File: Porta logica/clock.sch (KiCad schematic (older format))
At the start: 12 parts, among them P5 Clock, U6 74HC00, U7 LM555N

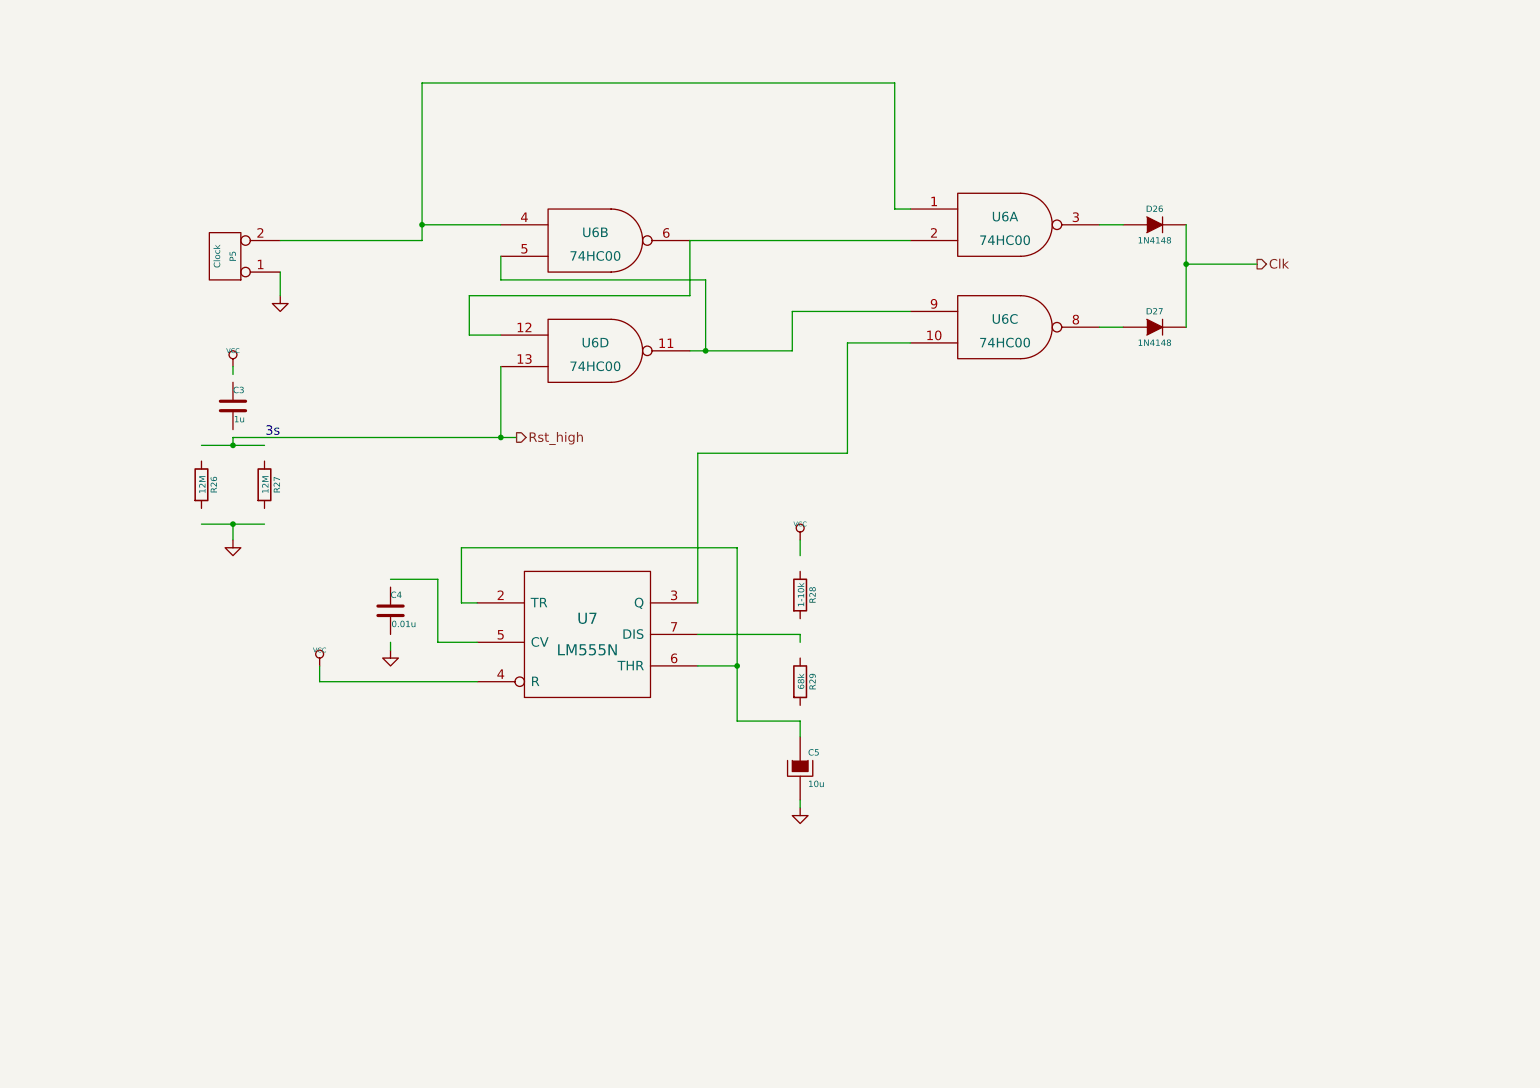
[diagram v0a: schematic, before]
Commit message: correzione bug, migliorie grafiche
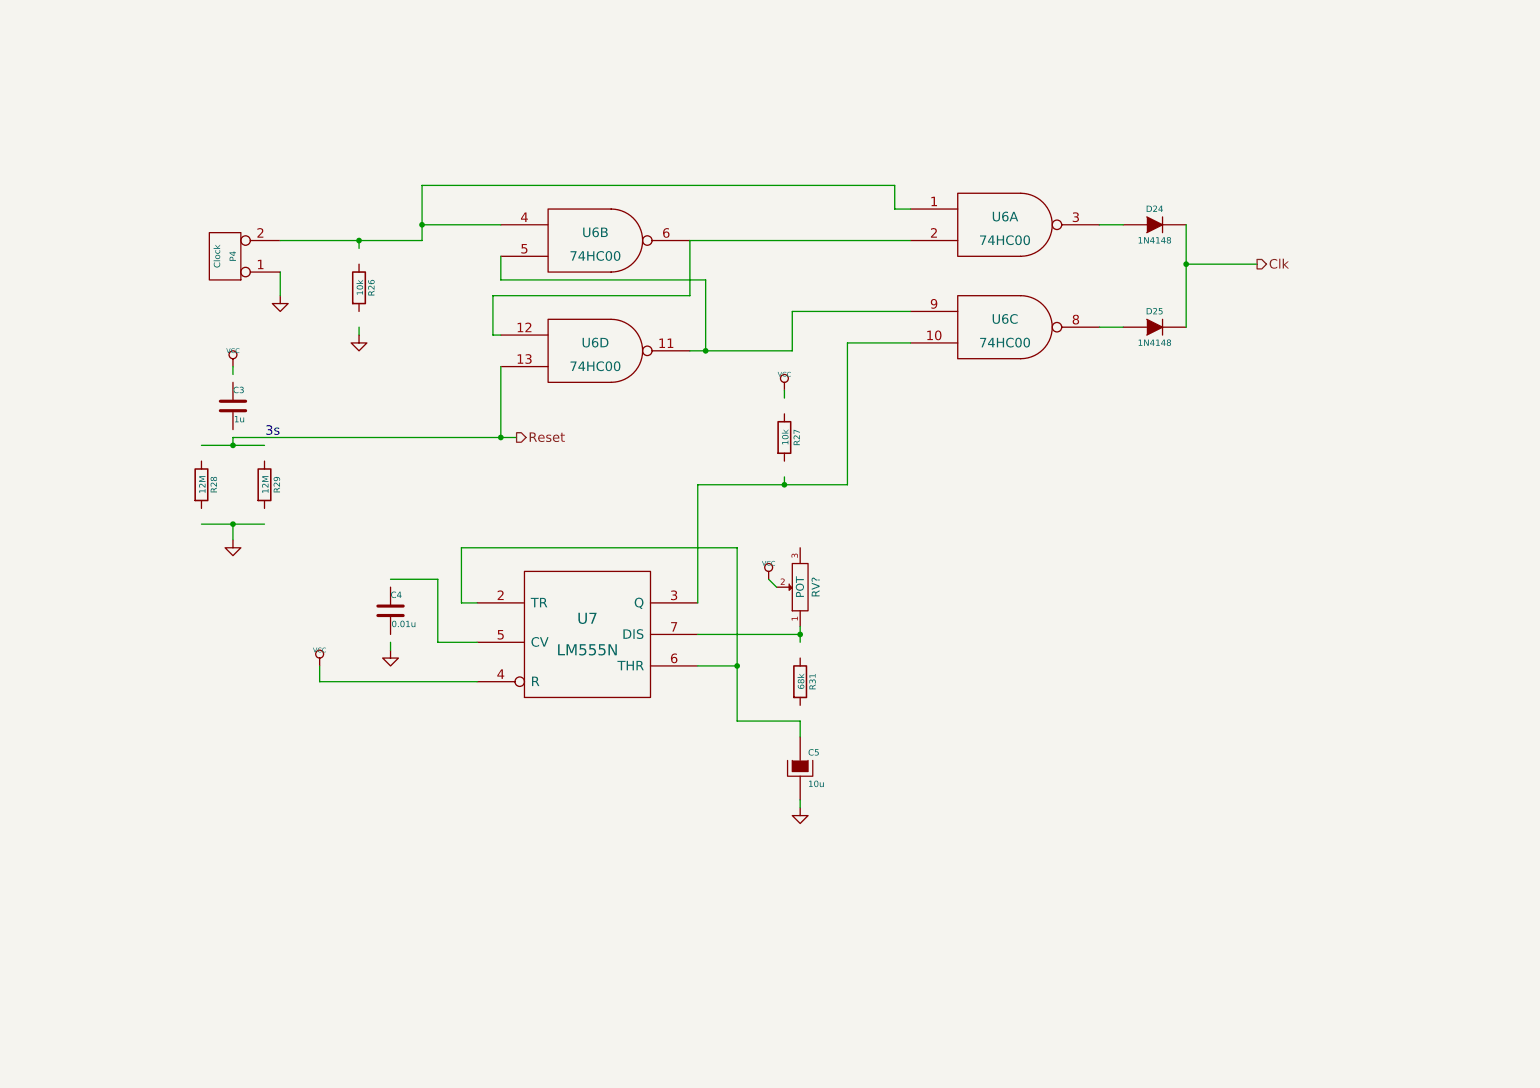
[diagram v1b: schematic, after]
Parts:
- removed R28: 1-10k, ~, symbol R
- added R26, R27: 10k, ~, symbol R
- added RV?: POT, ~, symbol POT
- renumbered D26 to D24, D27 to D25, P5 to P4, R26 to R28, R27 to R29, R29 to R31
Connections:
- net labels added: Reset
- net labels removed: Rst_high
- wire segments 50 -> 54
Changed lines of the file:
@@
 $Descr A4 11693 8268
 encoding utf-8
-Sheet 3 3
+Sheet 2 3
 Title ""
 Date "20 may 2015"
@@
 $EndComp
 $Comp
-L VCC #PWR021
+L VCC #PWR019
 U 1 1 555C3841
 P 3250 4650
-F 0 "#PWR021" H 3250 4750 30  0001 C CNN
+F 0 "#PWR019" H 3250 4750 30  0001 C CNN
 F 1 "VCC" H 3250 4750 30  0000 C CNN
 F 2 "" H 3250 4650 60  0000 C CNN
@@
 $EndComp
 $Comp
-L GND #PWR022
+L GND #PWR020
 U 1 1 555C384D
 P 3700 4550
-F 0 "#PWR022" H 3700 4550 30  0001 C CNN
+F 0 "#PWR020" H 3700 4550 30  0001 C CNN
 F 1 "GND" H 3700 4480 30  0001 C CNN
 F 2 "" H 3700 4550 60  0000 C CNN
@@
 $EndComp
 $Comp
-L R R29
+L R R31
 U 1 1 555C3853
 P 6300 4750
-F 0 "R29" V 6380 4750 40  0000 C CNN
+F 0 "R31" V 6380 4750 40  0000 C CNN
 F 1 "68k" V 6307 4751 40  0000 C CNN
 F 2 "~" V 6230 4750 30  0000 C CNN
 F 3 "~" H 6300 4750 30  0000 C CNN
 	1    6300 4750
-	1    0    0    -1
-$EndComp
-$Comp
-L R R28
-U 1 1 555C3859
-P 6300 4200
-F 0 "R28" V 6380 4200 40  0000 C CNN
-F 1 "1-10k" V 6307 4201 40  0000 C CNN
-F 2 "~" V 6230 4200 30  0000 C CNN
-F 3 "~" H 6300 4200 30  0000 C CNN
-	1    6300 4200
 	1    0    0    -1
 $EndComp
@@
 $EndComp
 $Comp
-L VCC #PWR023
+L VCC #PWR021
 U 1 1 555C3865
-P 6300 3850
-F 0 "#PWR023" H 6300 3950 30  0001 C CNN
-F 1 "VCC" H 6300 3950 30  0000 C CNN
-F 2 "" H 6300 3850 60  0000 C CNN
-F 3 "" H 6300 3850 60  0000 C CNN
-	1    6300 3850
-	1    0    0    -1
-$EndComp
-$Comp
-L GND #PWR024
+P 6100 4100
+F 0 "#PWR021" H 6100 4200 30  0001 C CNN
+F 1 "VCC" H 6100 4200 30  0000 C CNN
+F 2 "" H 6100 4100 60  0000 C CNN
+F 3 "" H 6100 4100 60  0000 C CNN
+	1    6100 4100
+	1    0    0    -1
+$EndComp
+$Comp
+L GND #PWR022
 U 1 1 555C386B
 P 6300 5550
-F 0 "#PWR024" H 6300 5550 30  0001 C CNN
+F 0 "#PWR022" H 6300 5550 30  0001 C CNN
 F 1 "GND" H 6300 5480 30  0001 C CNN
 F 2 "" H 6300 5550 60  0000 C CNN
@@
 	6300 5000 6300 5100
 Wire Wire Line
-	6300 4500 6300 4450
+	6300 4400 6300 4500
 Wire Wire Line
 	6300 5500 6300 5550
 Wire Wire Line
-	6300 3950 6300 3850
+	6150 4150 6100 4100
 Wire Wire Line
 	6300 4450 5650 4450
@@
 Connection ~ 5900 4650
 Wire Wire Line
-	5650 3300 5650 4250
-$Comp
-L CONN_2 P5
+	5650 3500 5650 4250
+$Comp
+L CONN_2 P4
 U 1 1 555C3887
 P 2650 2050
-F 0 "P5" V 2600 2050 40  0000 C CNN
+F 0 "P4" V 2600 2050 40  0000 C CNN
 F 1 "Clock" V 2700 2050 40  0000 C CNN
 F 2 "" H 2650 2050 60  0000 C CNN
@@
 $EndComp
 $Comp
-L GND #PWR025
+L GND #PWR023
 U 1 1 555C5E35
 P 3000 2300
-F 0 "#PWR025" H 3000 2300 30  0001 C CNN
+F 0 "#PWR023" H 3000 2300 30  0001 C CNN
 F 1 "GND" H 3000 2230 30  0001 C CNN
 F 2 "" H 3000 2300 60  0000 C CNN
@@
 	3900 1950 3000 1950
 Wire Wire Line
-	3900 950  3900 1950
-Wire Wire Line
-	3900 950  6900 950
-Wire Wire Line
-	6900 950  6900 1750
+	3900 1600 3900 1950
+Wire Wire Line
+	3900 1600 6900 1600
+Wire Wire Line
+	6900 1600 6900 1750
 Wire Wire Line
 	6900 1750 7000 1750
@@
 	5600 1950 5600 2300
 Wire Wire Line
-	5600 2300 4200 2300
-Wire Wire Line
-	4200 2300 4200 2550
-Wire Wire Line
-	4200 2550 4400 2550
+	5600 2300 4350 2300
+Wire Wire Line
+	4350 2300 4350 2550
+Wire Wire Line
+	4350 2550 4400 2550
 Wire Wire Line
 	4400 2050 4400 2200
@@
 	7000 2600 6600 2600
 Wire Wire Line
-	6600 2600 6600 3300
-Wire Wire Line
-	6600 3300 5650 3300
-$Comp
-L VCC #PWR026
+	6600 2600 6600 3500
+Wire Wire Line
+	6600 3500 5650 3500
+$Comp
+L VCC #PWR024
 U 1 1 555C5F80
 P 2700 2750
-F 0 "#PWR026" H 2700 2850 30  0001 C CNN
+F 0 "#PWR024" H 2700 2850 30  0001 C CNN
 F 1 "VCC" H 2700 2850 30  0000 C CNN
 F 2 "" H 2700 2750 60  0000 C CNN
@@
 $EndComp
 $Comp
-L GND #PWR027
+L GND #PWR025
 U 1 1 555C5F8F
 P 2700 3850
-F 0 "#PWR027" H 2700 3850 30  0001 C CNN
+F 0 "#PWR025" H 2700 3850 30  0001 C CNN
 F 1 "GND" H 2700 3780 30  0001 C CNN
 F 2 "" H 2700 3850 60  0000 C CNN
@@
 Clk
 Text HLabel 4500 3200 2    60   Output ~ 0
-Rst_high
+Reset
 Connection ~ 4400 3200
 $Comp
-L DIODE D26
+L DIODE D24
 U 1 1 555C7B93
 P 8550 1850
-F 0 "D26" H 8550 1950 40  0000 C CNN
+F 0 "D24" H 8550 1950 40  0000 C CNN
 F 1 "1N4148" H 8550 1750 40  0000 C CNN
 F 2 "~" H 8550 1850 60  0000 C CNN
@@
 $EndComp
 $Comp
-L DIODE D27
+L DIODE D25
 U 1 1 555C7BA5
 P 8550 2500
-F 0 "D27" H 8550 2600 40  0000 C CNN
+F 0 "D25" H 8550 2600 40  0000 C CNN
 F 1 "1N4148" H 8550 2400 40  0000 C CNN
 F 2 "~" H 8550 2500 60  0000 C CNN
@@
 	8200 2500 8350 2500
 Wire Wire Line
-	8750 2500 8750 1850
+	8750 1850 8750 2500
 Wire Wire Line
 	9200 2100 8750 2100
 Connection ~ 8750 2100
 $Comp
-L R R27
+L R R29
 U 1 1 555C7D7C
 P 2900 3500
-F 0 "R27" V 2980 3500 40  0000 C CNN
+F 0 "R29" V 2980 3500 40  0000 C CNN
 F 1 "12M" V 2907 3501 40  0000 C CNN
 F 2 "~" V 2830 3500 30  0000 C CNN
@@
 $EndComp
 $Comp
-L R R26
+L R R28
 U 1 1 555C7D82
 P 2500 3500
-F 0 "R26" V 2580 3500 40  0000 C CNN
+F 0 "R28" V 2580 3500 40  0000 C CNN
 F 1 "12M" V 2507 3501 40  0000 C CNN
 F 2 "~" V 2430 3500 30  0000 C CNN
@@
 	2500 3250 2900 3250
 Wire Wire Line
-	2900 3750 2500 3750
+	2500 3750 2900 3750
 Connection ~ 2700 3250
 Connection ~ 2700 3750
 Text Notes 3000 3200 2    60   ~ 0
 3s
+$Comp
+L R R27
+U 1 1 555CE354
+P 6200 3200
+F 0 "R27" V 6280 3200 40  0000 C CNN
+F 1 "10k" V 6207 3201 40  0000 C CNN
+F 2 "~" V 6130 3200 30  0000 C CNN
+F 3 "~" H 6200 3200 30  0000 C CNN
+	1    6200 3200
+	1    0    0    -1
+$EndComp
+$Comp
+L VCC #PWR026
+U 1 1 555CE368
+P 6200 2900
+F 0 "#PWR026" H 6200 3000 30  0001 C CNN
+F 1 "VCC" H 6200 3000 30  0000 C CNN
+F 2 "" H 6200 2900 60  0000 C CNN
+F 3 "" H 6200 2900 60  0000 C CNN
+	1    6200 2900
+	1    0    0    -1
+$EndComp
+Wire Wire Line
+	6200 2900 6200 2950
+$Comp
+L GND #PWR027
+U 1 1 555CE3B7
+P 3500 2550
+F 0 "#PWR027" H 3500 2550 30  0001 C CNN
+F 1 "GND" H 3500 2480 30  0001 C CNN
+F 2 "" H 3500 2550 60  0000 C CNN
+F 3 "" H 3500 2550 60  0000 C CNN
+	1    3500 2550
+	1    0    0    -1
+$EndComp
+$Comp
+L R R26
+U 1 1 555CE3C6
+P 3500 2250
+F 0 "R26" V 3580 2250 40  0000 C CNN
+F 1 "10k" V 3507 2251 40  0000 C CNN
+F 2 "~" V 3430 2250 30  0000 C CNN
+F 3 "~" H 3500 2250 30  0000 C CNN
+	1    3500 2250
+	1    0    0    -1
+$EndComp
+Wire Wire Line
+	3500 2500 3500 2550
+Wire Wire Line
+	3500 2000 3500 1950
+Connection ~ 3500 1950
+Wire Wire Line
+	6200 3450 6200 3500
+Connection ~ 6200 3500
+$Comp
+L POT RV?
+U 1 1 555D485F
+P 6300 4150
+F 0 "RV?" H 6300 4050 50  0000 C CNN
+F 1 "POT" H 6300 4150 50  0000 C CNN
+F 2 "~" H 6300 4150 60  0000 C CNN
+F 3 "~" H 6300 4150 60  0000 C CNN
+	1    6300 4150
+	0    -1   -1   0
+$EndComp
+Connection ~ 6300 4450
 $EndSCHEMATC

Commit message: Riordinato tutto lo schematico, eliminato power
Il contenuto di power.sch sta nello schematico principale. Fixato anche
il latch "fatto in casa", è default basso, non alto!
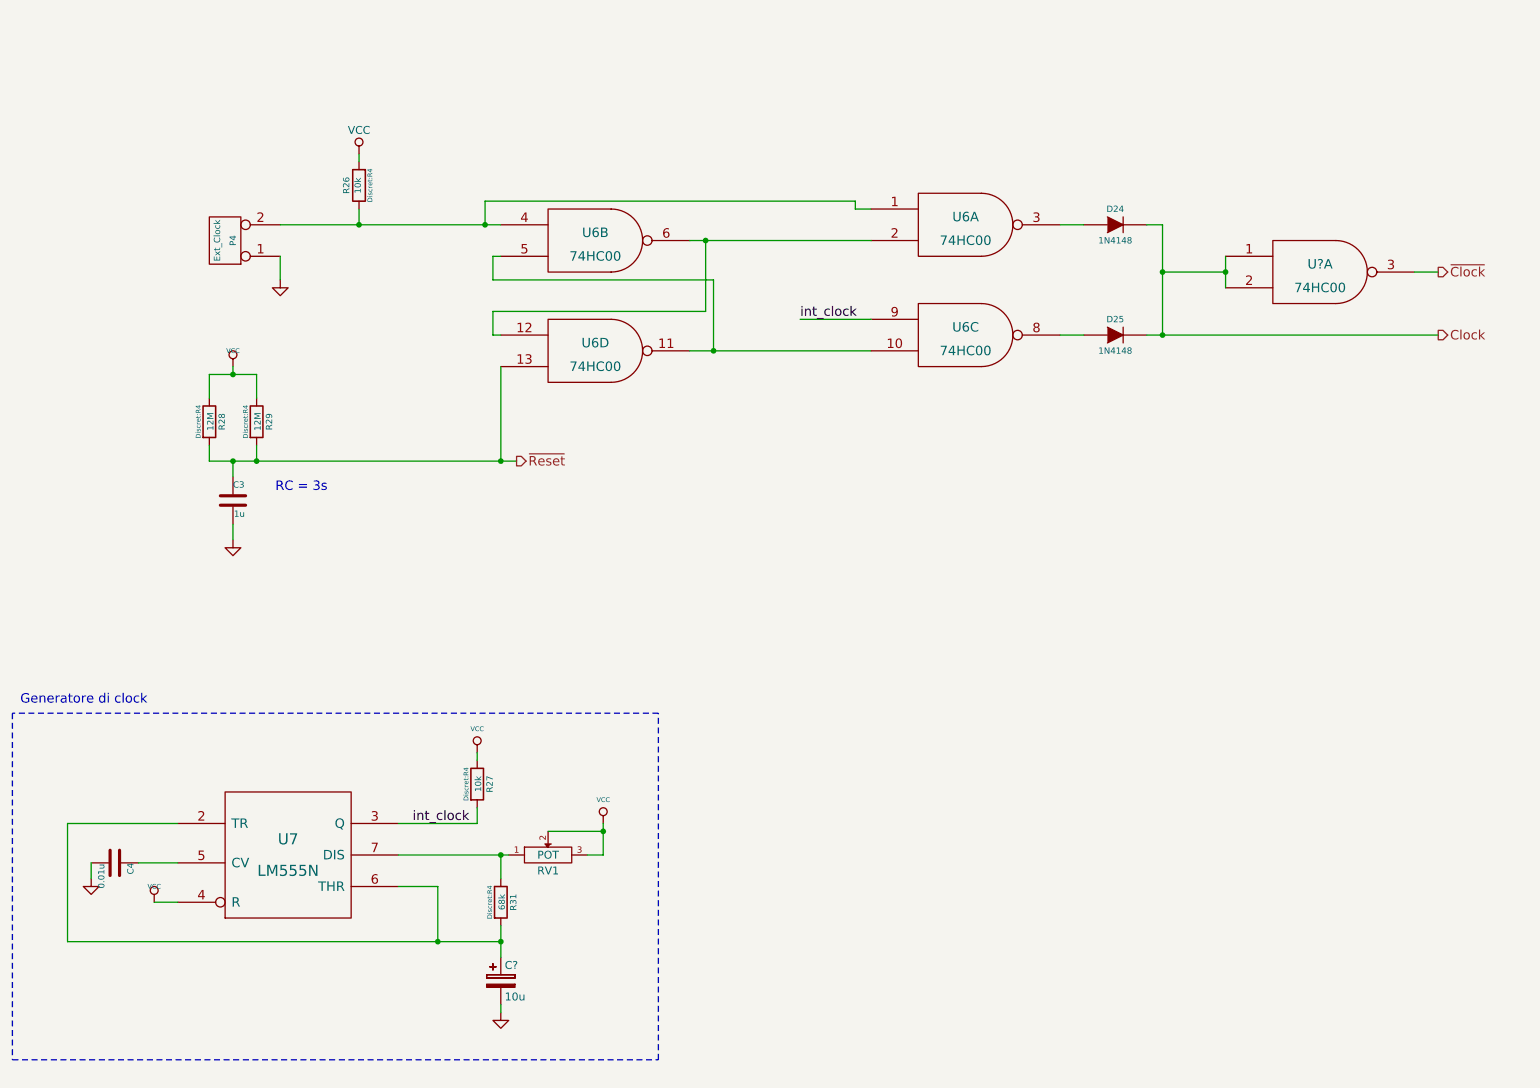
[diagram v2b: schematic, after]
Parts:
- removed C5: 10u, ~, symbol CAPAPOL
- added C?: 10u, symbol CP
- added U?: 74HC00, Housings_SOIC:SOIC-14_3.9x8.7mm_Pitch1.27mm, symbol 74HC00
- C3, C4: footprint ~ -> Capacitors_Elko_ThroughHole:Elko_vert_11.2x6.3mm_RM2.5
- D24, D25: footprint ~ -> Diodes_ThroughHole:Diode_DO-35_SOD27_Horizontal_RM10
- P4: value Clock -> Ext_Clock; footprint (none) -> Pin_Headers:Pin_Header_Straight_1x02
- R26, R27, R28, R29, R31: footprint ~ -> Discret:R4
- RV1: renamed from RV?; footprint ~ -> Potentiometers:Potentiometer_Trimmer-Piher_PT15-B_vertical
- U6: footprint ~ -> Housings_SSOP:SSOP-14_5.3x6.2mm_Pitch0.65mm
- U7: footprint (none) -> Housings_SOIC:SOIC-8_3.9x4.9mm_Pitch1.27mm
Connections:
- net labels added: Clock, int_clock, ~Clock, ~Reset
- net labels removed: Clk, Reset
- wire segments 54 -> 71
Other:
- note added: "Generatore di clock"
- note added: "RC = 3s"
- note removed: "3s"
- moved on the sheet: C3, C4, D24, D25, P4, R26, R27, R28, R29, R31, RV1, U6A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
